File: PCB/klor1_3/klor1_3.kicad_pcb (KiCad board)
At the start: 2 copper layers, 160 x 118.2 mm, 85 parts, among them J1 MJ-4PP-9, J2 Haptic Buzz, SW1 SW_PUSH-MX_W_LED, SW10 SW_PUSH-MX_W_LED, SW11 SW_PUSH-MX_W_LED, SW12 SW_PUSH-MX_W_LED, SW13 SW_PUSH-MX_W_LED, SW14 SW_PUSH-MX_W_LED, SW15 SW_PUSH-MX_W_LED, SW16 SW_PUSH-MX_W_LED, SW17 SW_PUSH-MX_W_LED, SW18 RotaryEncoder_Switch, SW19 SW_PUSH-MX_W_LED, SW2 SW_PUSH-MX_W_LED, SW20 SW_PUSH-MX_W_LED, SW21 SW_PUSH-MX_W_LED, SW23 5Way-Tactile_K1-1506DN-01, SW3 SW_PUSH-MX_W_LED, SW4 SW_PUSH-MX_W_LED, SW5 SW_PUSH-MX_W_LED, SW6 SW_PUSH-MX_W_LED, SW7 SW_PUSH-MX_W_LED, SW8 SW_PUSH-MX_W_LED, SW9 SW_PUSH-MX_W_LED, U1 ProMicro

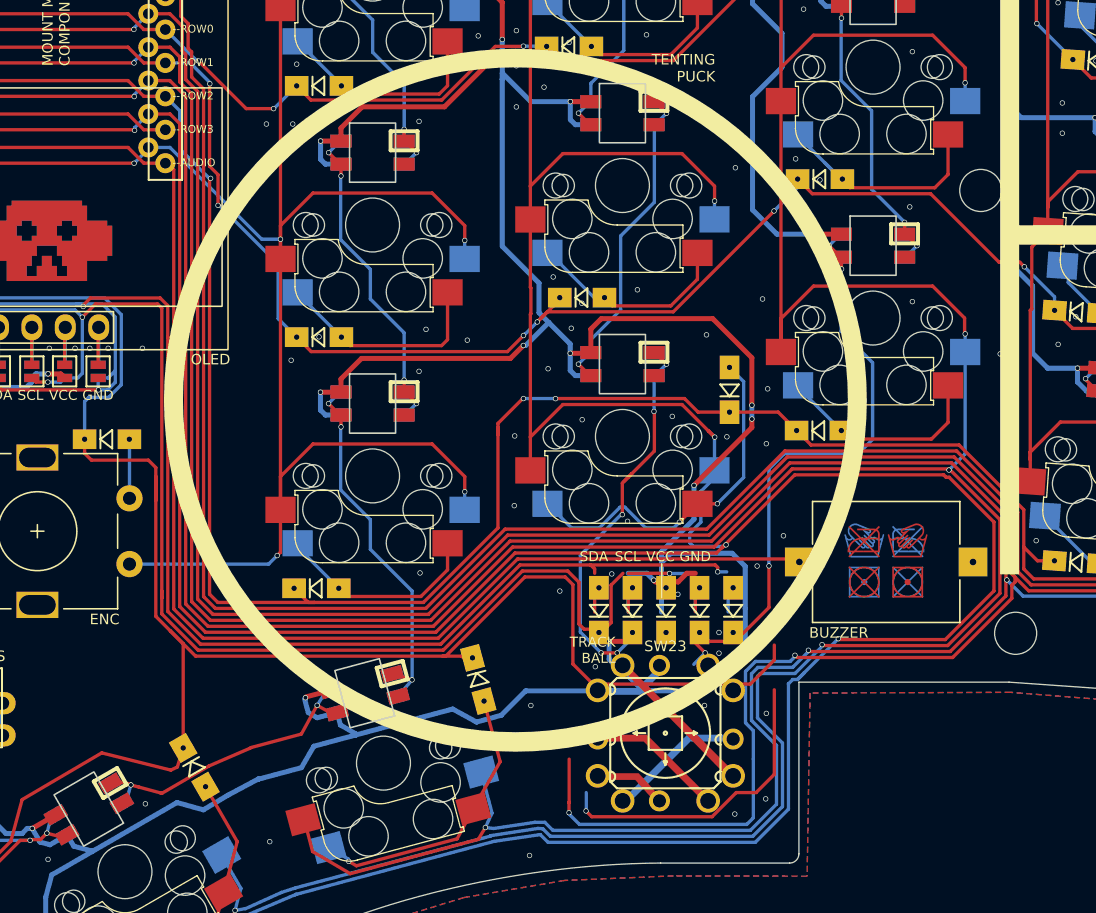
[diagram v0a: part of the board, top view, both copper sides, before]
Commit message: add routing of 5way switch to pcb
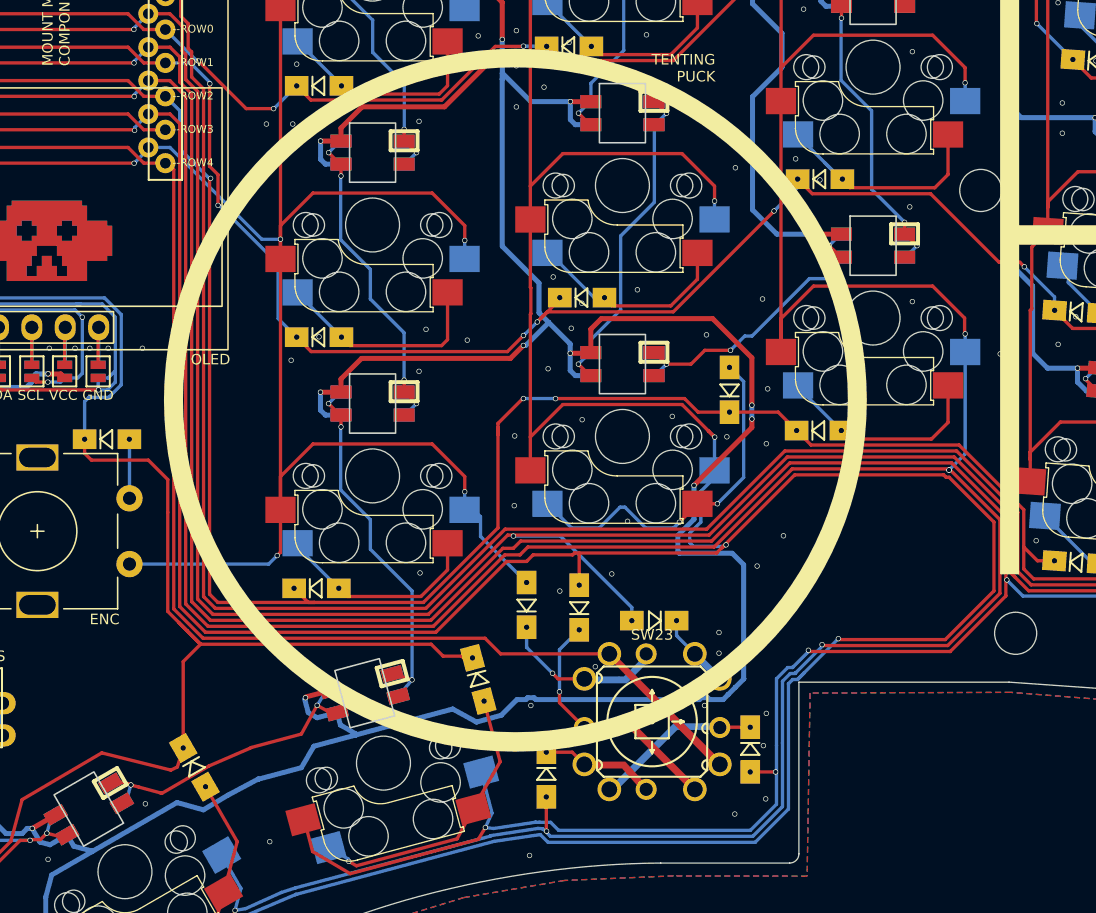
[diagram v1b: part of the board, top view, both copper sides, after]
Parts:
- removed BZ1: Buzzer, KLOR:Buzzer_Mallory_AST1109MLTRQ_reversible
- moved D25 15.5 mm to (134.3, 132.4), turned to -90 degrees
- moved D26 11.3 mm to (149.8, 130.6), turned to -90 degrees
- moved D27 6.05 mm to (142.5, 120.8), turned to 180 degrees
- moved D23 5.51 mm to (132.8, 119.5)
- moved D24 4.05 mm to (136.8, 119.8)
- moved SW23 1.34 mm to (142.3, 128.4)
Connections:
- net SW18A renamed col5
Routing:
- net AUDIO: track 101.9 -> 0.00 mm
- net row4: track 0.00 -> 85.6 mm
- net SCL: track 266.4 -> 185.1 mm, vias 4 -> 3
- net SDA: track 277.8 -> 200.1 mm, vias 5 -> 3
- net Net-(SW13B-DOUT): track 77.1 -> 22.3 mm, vias 9 -> 4
- net col1: track 310.8 -> 268.5 mm, vias 6 -> 5
- net row3: track 175.2 -> 137.6 mm
- net (no net): track 42.2 -> 12.7 mm, vias 3 -> 2
- net VCC: track 780.6 -> 767.5 mm, vias 32 -> 31
- net Net-(D24-K): track 0.00 -> 8.83 mm, vias 0 -> 1
- net Net-(D23-K): track 0.00 -> 6.91 mm, vias 0 -> 1
- net col5: track 145.9 -> 151.8 mm
- net GND: track 52.5 -> 46.9 mm, vias 139 -> 138
- net col2: track 337.1 -> 332.2 mm, vias 7 -> 8
- net Net-(D25-K): track 0.00 -> 3.27 mm
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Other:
- board text added: "--ROW4"
- board text removed: "--AUDIO"
- board text removed: "BUZZER"
- board text removed: "TRACK BALL"
